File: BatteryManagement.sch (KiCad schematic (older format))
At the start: 21 parts, among them J201 Bootstrap, U201 AP9211, U202 MCP73213T-A6BI_MF, U203 BQ29209DRBR

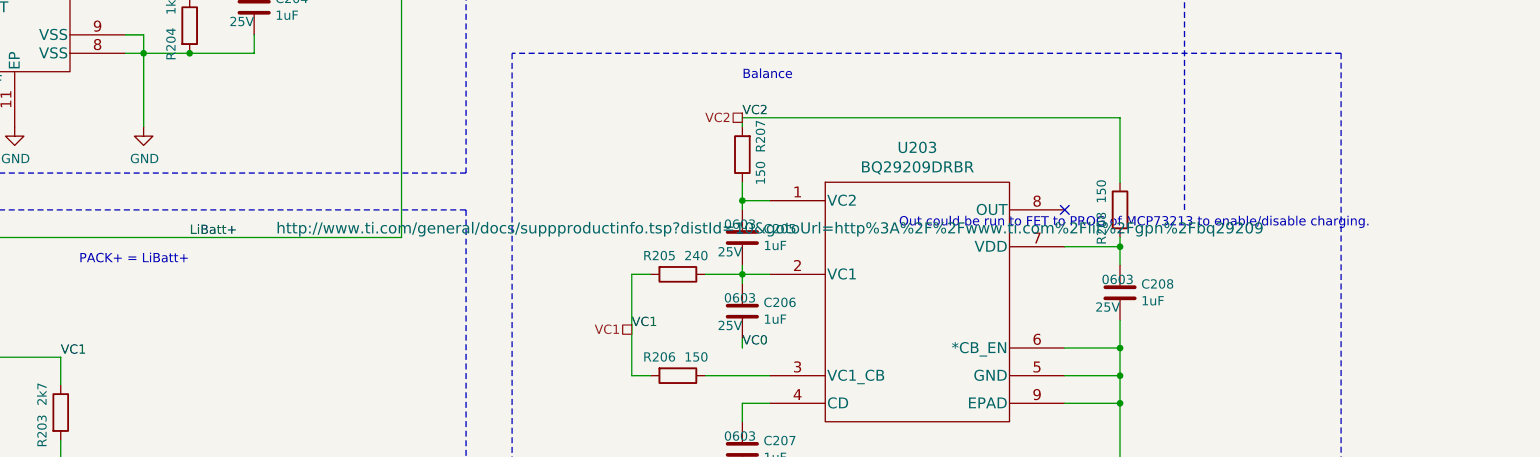
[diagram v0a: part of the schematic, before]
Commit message: Trying out layout, modifying solder pad footprint.
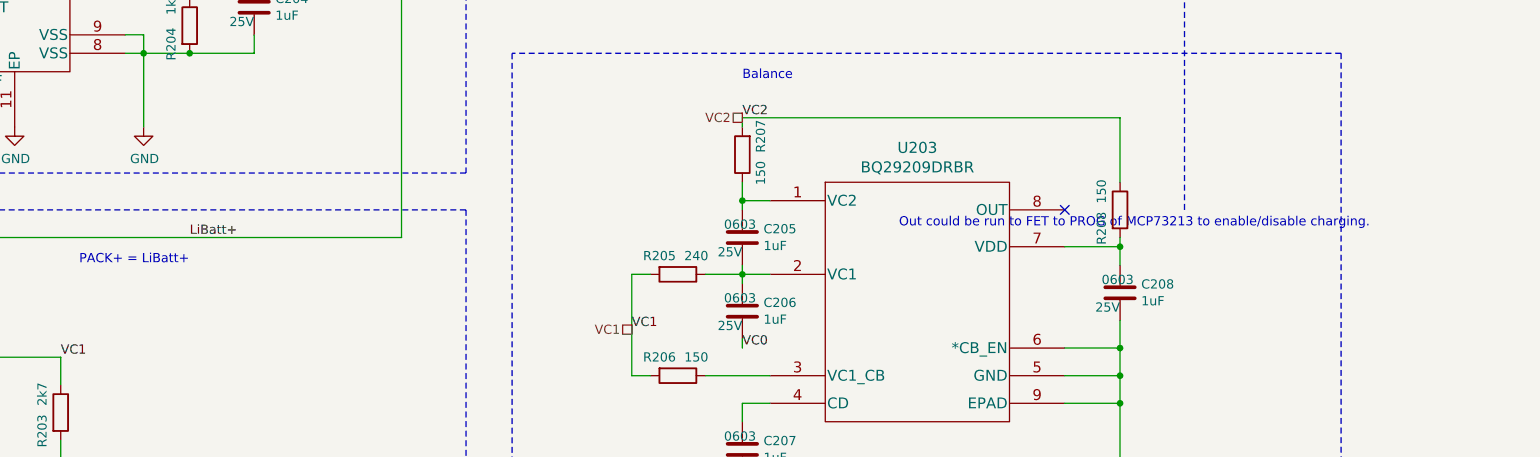
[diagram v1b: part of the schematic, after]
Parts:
- J201: footprint Pin_Headers:Pin_Header_Straight_1x02_Pitch2.54mm -> Pin_Headers:Pin_Header_Straight_1x02_Pitch1.27mm
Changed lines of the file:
@@
 F 0 "J201" V 2572 6080 50  0000 L CNN
 F 1 "Bootstrap" V 2663 6080 50  0000 L CNN
-F 2 "Pin_Headers:Pin_Header_Straight_1x02_Pitch2.54mm" H 2700 6000 50  0001 C CNN
+F 2 "Pin_Headers:Pin_Header_Straight_1x02_Pitch1.27mm" H 2700 6000 50  0001 C CNN
 F 3 "~" H 2700 6000 50  0001 C CNN
 	1    2700 6000
@@
 F 1 "BQ29209DRBR" H 8200 5431 60  0000 C CNN
 F 2 "libs:BQ29209DRBR" H 8200 4700 60  0001 C CNN
-F 3 "http://www.ti.com/general/docs/suppproductinfo.tsp?distId=10&gotoUrl=http%3A%2F%2Fwww.ti.com%2Flit%2Fgpn%2Fbq29209" H 7400 5100 60  0000 C CNN
+F 3 "http://www.ti.com/general/docs/suppproductinfo.tsp?distId=10&gotoUrl=http%3A%2F%2Fwww.ti.com%2Flit%2Fgpn%2Fbq29209" H 7400 5100 60  0001 C CNN
 F 4 "https://www.digikey.com/product-detail/en/texas-instruments/BQ29209DRBR/296-27677-1-ND/2350211" H 8200 4700 50  0001 C CNN "Link"
 F 5 "BQ29209DRBR" H 8200 4700 50  0001 C CNN "Mfg Part #"

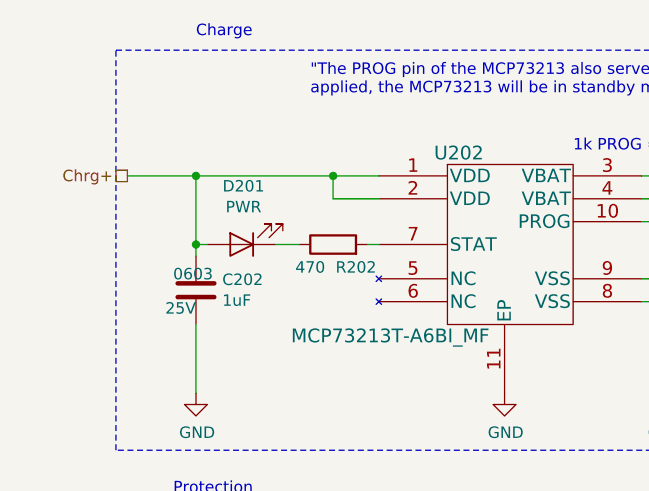
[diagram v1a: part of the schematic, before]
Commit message: Compacting blocks of layout.
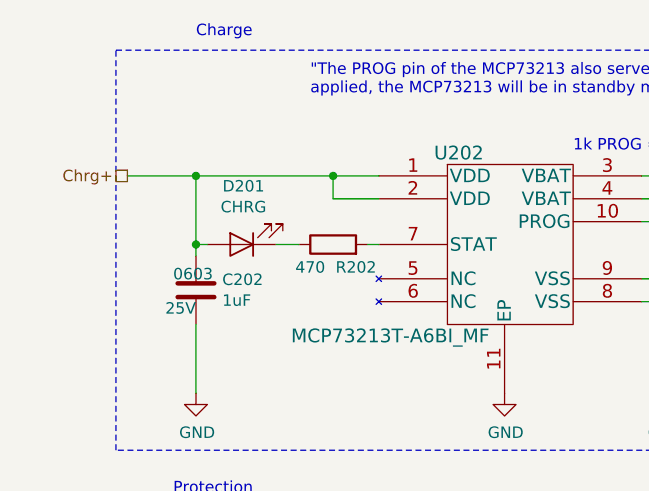
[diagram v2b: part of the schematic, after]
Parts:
- D201: value PWR -> CHRG
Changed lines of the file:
@@
 AR Path="/5DC297AB/5DE917F2" Ref="D201"  Part="1"
 F 0 "D201" H 2142 2845 50  0000 C CNN
-F 1 "PWR" H 2142 2936 50  0000 C CNN
+F 1 "CHRG" H 2142 2936 50  0000 C CNN
 F 2 "LEDs:LED_0603" H 2150 3100 50  0001 C CNN
 F 3 "~" H 2150 3100 50  0001 C CNN

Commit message: updated footprints to handsolder
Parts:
- C201, C202, C203, C204, C205, C206, C207, C208: footprint Capacitors_SMD:C_0603 -> Capacitor_SMD:C_0603_1608Metric_Pad1.05x0.95mm_HandSolder
- D201: footprint LEDs:LED_0603 -> LED_SMD:LED_0603_1608Metric_Pad1.05x0.95mm_HandSolder
- R201, R202, R203, R204, R205, R206, R207, R208: footprint Resistors_SMD:R_0603 -> Resistor_SMD:R_0603_1608Metric_Pad1.05x0.95mm_HandSolder
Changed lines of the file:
@@
 F 0 "C201" H 1915 5246 50  0000 L CNN
 F 1 "100nF" H 1915 5155 50  0000 L CNN
-F 2 "Capacitors_SMD:C_0603" H 1838 5050 50  0001 C CNN
+F 2 "Capacitor_SMD:C_0603_1608Metric_Pad1.05x0.95mm_HandSolder" H 1838 5050 50  0001 C CNN
 F 3 "~" H 1800 5200 50  0001 C CNN
 F 4 "0603" H 1700 5300 50  0000 L TNN "Package"
@@
 F 0 "R203" V 3450 5200 50  0000 C CNN
 F 1 "2k7" V 3450 5400 50  0000 C CNN
-F 2 "Resistors_SMD:R_0603" V 3480 5300 50  0001 C CNN
+F 2 "Resistor_SMD:R_0603_1608Metric_Pad1.05x0.95mm_HandSolder" V 3480 5300 50  0001 C CNN
 F 3 "~" H 3550 5300 50  0001 C CNN
 F 4 "0603" H 2250 -750 50  0001 C CNN "Package"
@@
 F 0 "R201" V 1700 4600 50  0000 C CNN
 F 1 "470" V 1700 4800 50  0000 C CNN
-F 2 "Resistors_SMD:R_0603" V 1730 4700 50  0001 C CNN
+F 2 "Resistor_SMD:R_0603_1608Metric_Pad1.05x0.95mm_HandSolder" V 1730 4700 50  0001 C CNN
 F 3 "~" H 1800 4700 50  0001 C CNN
 F 4 "0603" H 500 -1350 50  0001 C CNN "Package"
@@
 F 0 "D201" H 2142 2845 50  0000 C CNN
 F 1 "CHRG" H 2142 2936 50  0000 C CNN
-F 2 "LEDs:LED_0603" H 2150 3100 50  0001 C CNN
+F 2 "LED_SMD:LED_0603_1608Metric_Pad1.05x0.95mm_HandSolder" H 2150 3100 50  0001 C CNN
 F 3 "~" H 2150 3100 50  0001 C CNN
 F 4 "0603" H 1250 -2950 50  0001 C CNN "Package"
@@
 F 0 "R202" V 2450 3000 50  0000 C CNN
 F 1 "470" V 2450 3200 50  0000 C CNN
-F 2 "Resistors_SMD:R_0603" V 2480 3100 50  0001 C CNN
+F 2 "Resistor_SMD:R_0603_1608Metric_Pad1.05x0.95mm_HandSolder" V 2480 3100 50  0001 C CNN
 F 3 "~" H 2550 3100 50  0001 C CNN
 F 4 "0603" H 1250 -2950 50  0001 C CNN "Package"
@@
 F 0 "R204" V 4150 3100 50  0000 C CNN
 F 1 "1k" V 4150 3300 50  0000 C CNN
-F 2 "Resistors_SMD:R_0603" V 4180 3200 50  0001 C CNN
+F 2 "Resistor_SMD:R_0603_1608Metric_Pad1.05x0.95mm_HandSolder" V 4180 3200 50  0001 C CNN
 F 3 "~" H 4250 3200 50  0001 C CNN
 F 4 "0603" H 2950 -2850 50  0001 C CNN "Package"
@@
 F 0 "C204" H 4715 3146 50  0000 L CNN
 F 1 "1uF" H 4715 3055 50  0000 L CNN
-F 2 "Capacitors_SMD:C_0603" H 4638 2950 50  0001 C CNN
+F 2 "Capacitor_SMD:C_0603_1608Metric_Pad1.05x0.95mm_HandSolder" H 4638 2950 50  0001 C CNN
 F 3 "~" H 4600 3100 50  0001 C CNN
 F 4 "0603" H 4500 3200 50  0000 L TNN "Package"
@@
 F 0 "C202" H 2065 3346 50  0000 L CNN
 F 1 "1uF" H 2065 3255 50  0000 L CNN
-F 2 "Capacitors_SMD:C_0603" H 1988 3150 50  0001 C CNN
+F 2 "Capacitor_SMD:C_0603_1608Metric_Pad1.05x0.95mm_HandSolder" H 1988 3150 50  0001 C CNN
 F 3 "~" H 1950 3300 50  0001 C CNN
 F 4 "0603" H 1850 3400 50  0000 L TNN "Package"
@@
 F 0 "R208" V 9200 4100 50  0000 C CNN
 F 1 "150" V 9200 4300 50  0000 C CNN
-F 2 "Resistors_SMD:R_0603" V 9230 4200 50  0001 C CNN
+F 2 "Resistor_SMD:R_0603_1608Metric_Pad1.05x0.95mm_HandSolder" V 9230 4200 50  0001 C CNN
 F 3 "~" H 9300 4200 50  0001 C CNN
 F 4 "0603" H 8000 -1850 50  0001 C CNN "Package"
@@
 F 0 "C206" H 7365 4796 50  0000 L CNN
 F 1 "1uF" H 7365 4705 50  0000 L CNN
-F 2 "Capacitors_SMD:C_0603" H 7288 4600 50  0001 C CNN
+F 2 "Capacitor_SMD:C_0603_1608Metric_Pad1.05x0.95mm_HandSolder" H 7288 4600 50  0001 C CNN
 F 3 "~" H 7250 4750 50  0001 C CNN
 F 4 "0603" H 7150 4850 50  0000 L TNN "Package"
@@
 F 0 "C205" H 7365 4396 50  0000 L CNN
 F 1 "1uF" H 7365 4305 50  0000 L CNN
-F 2 "Capacitors_SMD:C_0603" H 7288 4200 50  0001 C CNN
+F 2 "Capacitor_SMD:C_0603_1608Metric_Pad1.05x0.95mm_HandSolder" H 7288 4200 50  0001 C CNN
 F 3 "~" H 7250 4350 50  0001 C CNN
 F 4 "0603" H 7150 4450 50  0000 L TNN "Package"
@@
 F 0 "C208" H 9415 4696 50  0000 L CNN
 F 1 "1uF" H 9415 4605 50  0000 L CNN
-F 2 "Capacitors_SMD:C_0603" H 9338 4500 50  0001 C CNN
+F 2 "Capacitor_SMD:C_0603_1608Metric_Pad1.05x0.95mm_HandSolder" H 9338 4500 50  0001 C CNN
 F 3 "~" H 9300 4650 50  0001 C CNN
 F 4 "0603" H 9200 4750 50  0000 L TNN "Package"
@@
 F 0 "R205" V 6800 4450 50  0000 C CNN
 F 1 "240" V 6800 4650 50  0000 C CNN
-F 2 "Resistors_SMD:R_0603" V 6830 4550 50  0001 C CNN
+F 2 "Resistor_SMD:R_0603_1608Metric_Pad1.05x0.95mm_HandSolder" V 6830 4550 50  0001 C CNN
 F 3 "~" H 6900 4550 50  0001 C CNN
 F 4 "0603" H 5600 -1500 50  0001 C CNN "Package"
@@
 F 0 "R206" V 6800 5000 50  0000 C CNN
 F 1 "150" V 6800 5200 50  0000 C CNN
-F 2 "Resistors_SMD:R_0603" V 6830 5100 50  0001 C CNN
+F 2 "Resistor_SMD:R_0603_1608Metric_Pad1.05x0.95mm_HandSolder" V 6830 5100 50  0001 C CNN
 F 3 "~" H 6900 5100 50  0001 C CNN
 F 4 "0603" H 5600 -950 50  0001 C CNN "Package"
@@
 F 0 "R207" V 7150 3800 50  0000 C CNN
 F 1 "150" V 7150 4000 50  0000 C CNN
-F 2 "Resistors_SMD:R_0603" V 7180 3900 50  0001 C CNN
+F 2 "Resistor_SMD:R_0603_1608Metric_Pad1.05x0.95mm_HandSolder" V 7180 3900 50  0001 C CNN
 F 3 "~" H 7250 3900 50  0001 C CNN
 F 4 "0603" H 5950 -2150 50  0001 C CNN "Package"
@@
 F 0 "C207" H 7365 5546 50  0000 L CNN
 F 1 "1uF" H 7365 5455 50  0000 L CNN
-F 2 "Capacitors_SMD:C_0603" H 7288 5350 50  0001 C CNN
+F 2 "Capacitor_SMD:C_0603_1608Metric_Pad1.05x0.95mm_HandSolder" H 7288 5350 50  0001 C CNN
 F 3 "~" H 7250 5500 50  0001 C CNN
 F 4 "0603" H 7150 5600 50  0000 L TNN "Package"
@@
 F 0 "C203" H 2315 5996 50  0000 L CNN
 F 1 "1uF" H 2315 5905 50  0000 L CNN
-F 2 "Capacitors_SMD:C_0603" H 2238 5800 50  0001 C CNN
+F 2 "Capacitor_SMD:C_0603_1608Metric_Pad1.05x0.95mm_HandSolder" H 2238 5800 50  0001 C CNN
 F 3 "~" H 2200 5950 50  0001 C CNN
 F 4 "0603" H 2100 6050 50  0000 L TNN "Package"

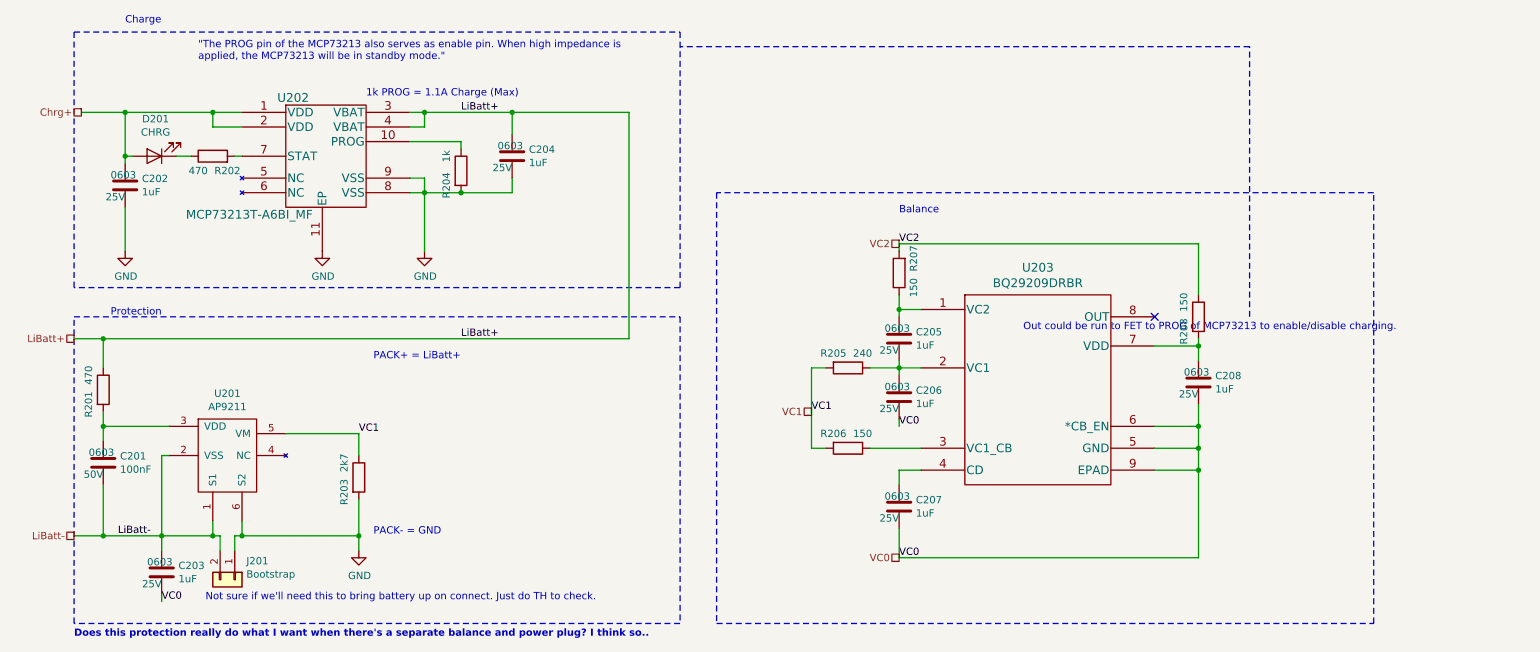
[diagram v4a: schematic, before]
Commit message: Remove the LiPo OC protection, fuse & RP will be sufficient when used with balance & charge OV cutoff. That change is in here too. Closes #17, closes #22.
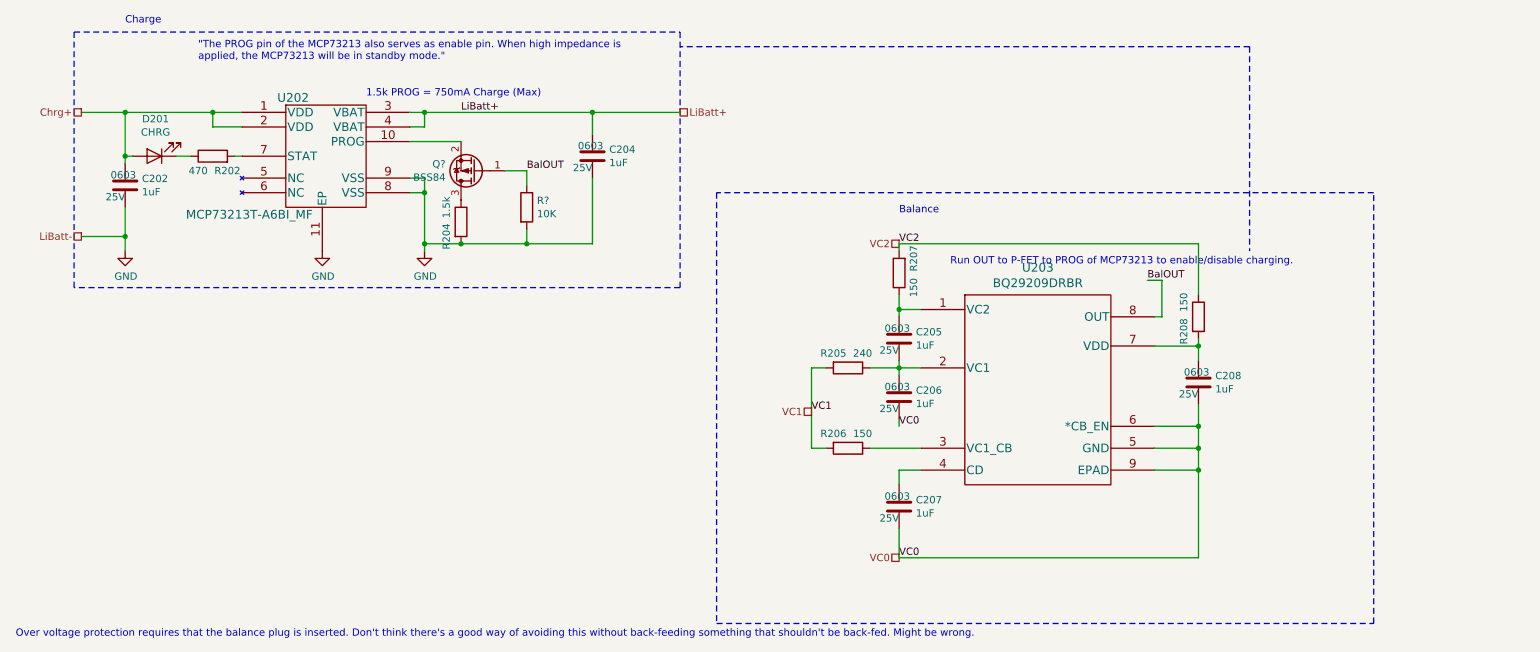
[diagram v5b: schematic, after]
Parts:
- removed C201: 100nF, Capacitor_SMD:C_0603_1608Metric_Pad1.05x0.95mm_HandSolder, symbol Device:C
- removed C203: 1uF, Capacitor_SMD:C_0603_1608Metric_Pad1.05x0.95mm_HandSolder, symbol Device:C
- removed J201: Bootstrap, Pin_Headers:Pin_Header_Straight_1x02_Pitch1.27mm, symbol Connector_Generic:Conn_01x02
- removed R201: 470, Resistor_SMD:R_0603_1608Metric_Pad1.05x0.95mm_HandSolder, symbol Device:R
- removed R203: 2k7, Resistor_SMD:R_0603_1608Metric_Pad1.05x0.95mm_HandSolder, symbol Device:R
- removed U201: AP9211, libs:6-UDFN-Exposed-Pad, symbol dingo-hat:AP9211
- added Q?: BSS84, TO_SOT_Packages_SMD:SOT-23, symbol Transistor_FET:BSS84
- added R?: 10K, Resistor_SMD:R_0603_1608Metric_Pad1.05x0.95mm_HandSolder, symbol Device:R
- R204: value 1k -> 1.5k
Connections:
- net GND: now also R?.2
- net at U202.10 (PROG): now also Q?.2 (S); no longer R204.1
- net BalOUT: now reaches U203.8 (OUT)
- net BalOUT: now also Q?.1 (G), R?.1
- new net: Q?.3 (D), R204.1
- no-connect marks 1 -> 0
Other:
- note added: "1.5k PROG = 750mA Charge (Max)"
- note added: "Over voltage protection requires that the balance plug is inserted. Don't think there's a good way of avoiding this without back-feeding something that shouldn't be back-fed. Might be wrong."
- note added: "Run OUT to P-FET to PROG of MCP73213 to enable/disable charging."
- note removed: "1k PROG = 1.1A Charge (Max)"
- note removed: "Does this protection really do what I want when there's a separate balance and power plug? I think so.."
- note removed: "Not sure if we'll need this to bring battery up on connect. Just do TH to check."
- note removed: "Out could be run to FET to PROG of MCP73213 to enable/disable charging."
- note removed: "PACK+ = LiBatt+"
- note removed: "PACK- = GND"
- note removed: "Protection"
- moved on the sheet: C204, R204

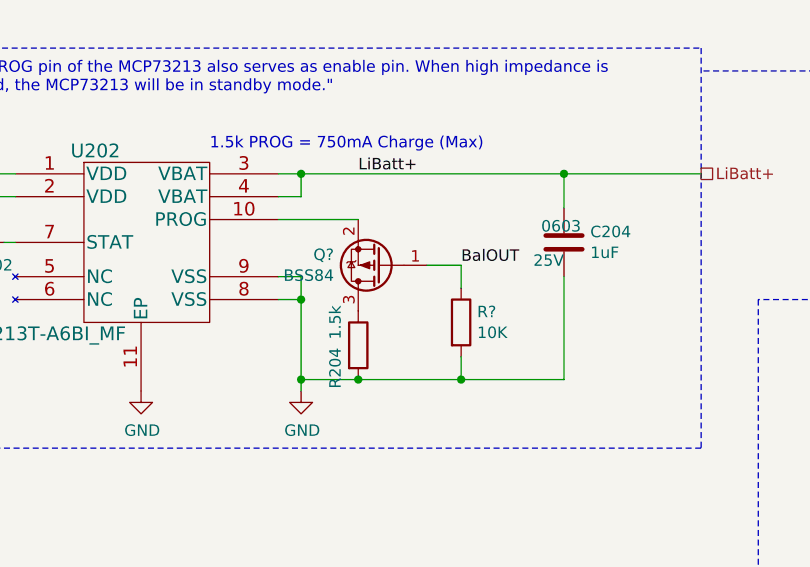
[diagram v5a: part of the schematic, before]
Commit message: Changing barrel jack to be 2.1ID, 5.5OD. Needs double check to close issue (28).
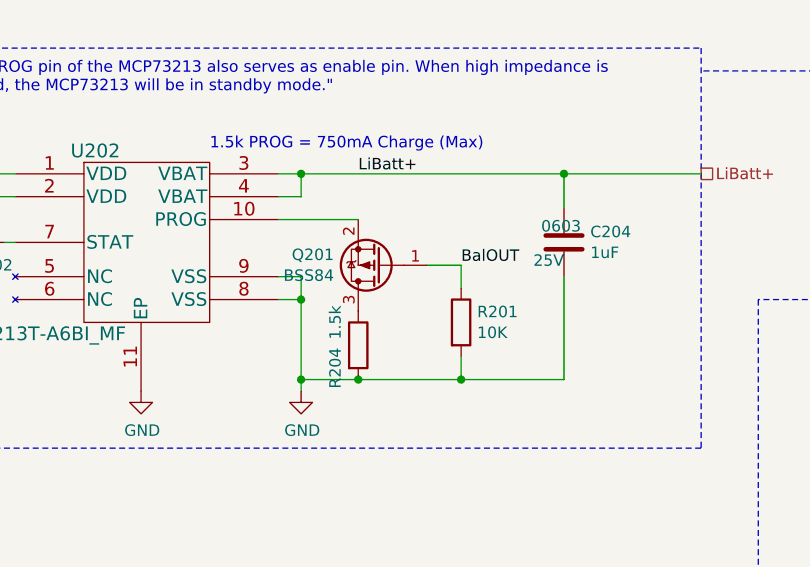
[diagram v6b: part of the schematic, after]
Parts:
- gave numbers to parts that had none: 2
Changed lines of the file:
@@
 	1950 3650 1950 3750
 $Comp
-L Transistor_FET:BSS84 Q?
+L Transistor_FET:BSS84 Q201
 U 1 1 5DE58FCE
 P 4350 3200
-F 0 "Q?" H 4556 3154 50  0000 L CNN
+F 0 "Q201" H 4556 3154 50  0000 L CNN
 F 1 "BSS84" H 4556 3245 50  0000 L CNN
 F 2 "TO_SOT_Packages_SMD:SOT-23" H 4550 3125 50  0001 L CIN
@@
 P 4700 3450
 AR Path="/5DE6B36C" Ref="R?"  Part="1"
-AR Path="/5DC297AB/5DE6B36C" Ref="R?"  Part="1"
-F 0 "R?" H 4770 3496 50  0000 L CNN
+AR Path="/5DC297AB/5DE6B36C" Ref="R201"  Part="1"
+F 0 "R201" H 4770 3496 50  0000 L CNN
 F 1 "10K" H 4770 3405 50  0000 L CNN
 F 2 "Resistor_SMD:R_0603_1608Metric_Pad1.05x0.95mm_HandSolder" V 4630 3450 50  0001 C CNN

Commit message: Trying to add in the ultrasonics, other bits.
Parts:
- R201: footprint Resistor_SMD:R_0603_1608Metric_Pad1.05x0.95mm_HandSolder -> Resistors_SMD:R_0603_HandSoldering
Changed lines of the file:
@@
 F 0 "R201" H 4770 3496 50  0000 L CNN
 F 1 "10K" H 4770 3405 50  0000 L CNN
-F 2 "Resistor_SMD:R_0603_1608Metric_Pad1.05x0.95mm_HandSolder" V 4630 3450 50  0001 C CNN
+F 2 "Resistors_SMD:R_0603_HandSoldering" V 4630 3450 50  0001 C CNN
 F 3 "~" H 4700 3450 50  0001 C CNN
 F 4 "0603" H -4050 600 50  0001 C CNN "Package"
